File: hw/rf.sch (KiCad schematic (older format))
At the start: 3 parts, among them J8 SMA, U8 HM-TRP-869S

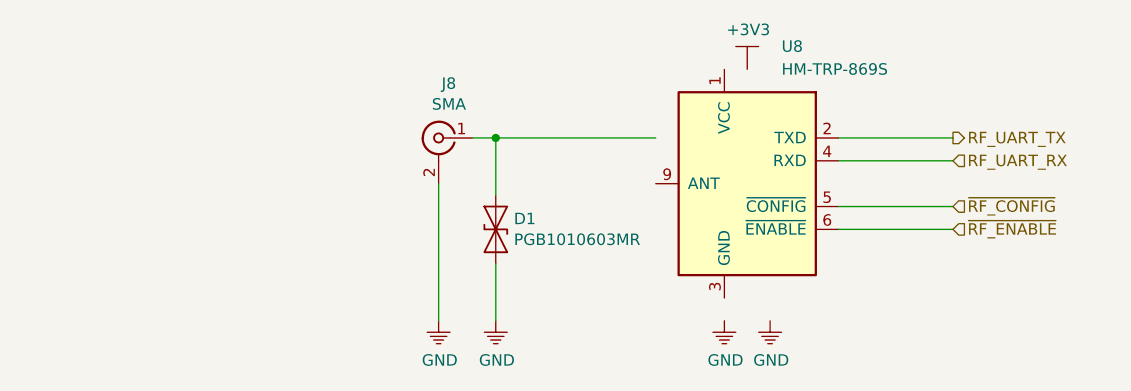
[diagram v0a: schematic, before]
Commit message: updated schematic added footptints
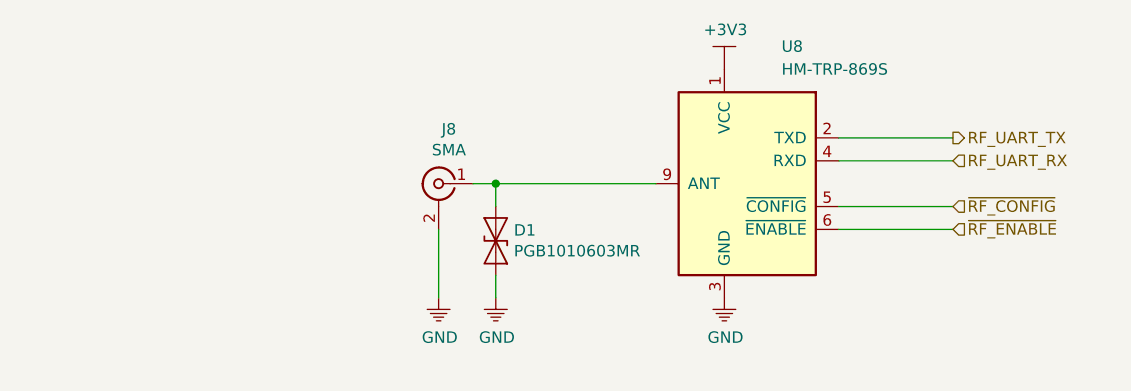
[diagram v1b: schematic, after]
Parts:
- D1: footprint (none) -> Diode_SMD:D_0603_1608Metric
- J8: footprint (none) -> Connector_Coaxial:SMA_Jack_Vertical
- U8: footprint (none) -> KLIB_RF_Module:HM-TRP-SMD
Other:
- moved on the sheet: D1, J8
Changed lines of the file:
@@
 F 0 "U8" H 4100 3200 50  0000 R CNN
 F 1 "HM-TRP-869S" H 4100 3100 50  0000 R CNN
-F 2 "" H 3750 2550 60  0000 C CNN
+F 2 "KLIB_RF_Module:HM-TRP-SMD" H 3750 2550 60  0001 C CNN
 F 3 "https://www.rcscomponents.kiev.ua/datasheets/HM-TRP_433.pdf" V 5050 2650 50  0001 C CNN
 	1    4250 2600
@@
 $EndComp
 $Comp
-L KLIB_Power:GND #PWR056
-U 1 1 5ABFB7B7
-P 4350 3200
-F 0 "#PWR056" H 4350 3000 50  0001 C CNN
-F 1 "GND" H 4355 3027 50  0000 C CNN
-F 2 "" H 4350 3200 50  0001 C CNN
-F 3 "" H 4350 3200 50  0001 C CNN
-	1    4350 3200
-	1    0    0    -1
-$EndComp
-$Comp
 L KLIB_Power:GND #PWR054
 U 1 1 5ABFB811
-P 4150 3200
-F 0 "#PWR054" H 4150 3000 50  0001 C CNN
-F 1 "GND" H 4155 3027 50  0000 C CNN
-F 2 "" H 4150 3200 50  0001 C CNN
-F 3 "" H 4150 3200 50  0001 C CNN
-	1    4150 3200
+P 4150 3100
+F 0 "#PWR054" H 4150 2900 50  0001 C CNN
+F 1 "GND" H 4155 2927 50  0000 C CNN
+F 2 "" H 4150 3100 50  0001 C CNN
+F 3 "" H 4150 3100 50  0001 C CNN
+	1    4150 3100
 	1    0    0    -1
 $EndComp
@@
 L KLIB_Power:+3V3 #PWR055
 U 1 1 5ABFB986
-P 4250 2100
-F 0 "#PWR055" H 4250 1800 50  0001 C CNN
-F 1 "+3V3" H 4255 2273 50  0000 C CNN
-F 2 "" H 4250 2100 50  0001 C CNN
-F 3 "" H 4250 2100 50  0001 C CNN
-	1    4250 2100
+P 4150 2100
+F 0 "#PWR055" H 4150 1800 50  0001 C CNN
+F 1 "+3V3" H 4155 2273 50  0000 C CNN
+F 2 "" H 4150 2100 50  0001 C CNN
+F 3 "" H 4150 2100 50  0001 C CNN
+	1    4150 2100
 	1    0    0    -1
 $EndComp
@@
 L Connector_Specialized:Conn_Coaxial J8
 U 1 1 5ABFBD92
-P 2900 2400
-F 0 "J8" H 2855 2638 50  0000 C CNN
-F 1 "SMA" H 2855 2547 50  0000 C CNN
-F 2 "" H 2900 2400 50  0001 C CNN
-F 3 "" H 2900 2400 50  0001 C CNN
-	1    2900 2400
+P 2900 2600
+F 0 "J8" H 2855 2838 50  0000 C CNN
+F 1 "SMA" H 2855 2747 50  0000 C CNN
+F 2 "Connector_Coaxial:SMA_Jack_Vertical" H 2900 2600 50  0001 C CNN
+F 3 "" H 2900 2600 50  0001 C CNN
+	1    2900 2600
 	-1   0    0    -1
 $EndComp
@@
 L KLIB_Power:GND #PWR052
 U 1 1 5ABFC6C3
-P 2900 3200
-F 0 "#PWR052" H 2900 3000 50  0001 C CNN
-F 1 "GND" H 2905 3027 50  0000 C CNN
-F 2 "" H 2900 3200 50  0001 C CNN
-F 3 "" H 2900 3200 50  0001 C CNN
-	1    2900 3200
+P 2900 3100
+F 0 "#PWR052" H 2900 2900 50  0001 C CNN
+F 1 "GND" H 2905 2927 50  0000 C CNN
+F 2 "" H 2900 3100 50  0001 C CNN
+F 3 "" H 2900 3100 50  0001 C CNN
+	1    2900 3100
 	1    0    0    -1
 $EndComp
 Wire Wire Line
-	2900 3200 2900 2600
+	2900 3100 2900 2800
 Wire Wire Line
-	3050 2400 3150 2400
+	3050 2600 3150 2600
 $Comp
 L Device:D_TVS D1
 U 1 1 5ABFDC8A
-P 3150 2800
-F 0 "D1" V 3104 2879 50  0000 L CNN
-F 1 "PGB1010603MR" V 3195 2879 50  0000 L CNN
-F 2 "" H 3150 2800 50  0001 C CNN
-F 3 "~" H 3150 2800 50  0001 C CNN
-	1    3150 2800
+P 3150 2850
+F 0 "D1" V 3104 2929 50  0000 L CNN
+F 1 "PGB1010603MR" V 3195 2929 50  0000 L CNN
+F 2 "Diode_SMD:D_0603_1608Metric" H 3150 2850 50  0001 C CNN
+F 3 "~" H 3150 2850 50  0001 C CNN
+	1    3150 2850
 	0    1    1    0
 $EndComp
@@
 L KLIB_Power:GND #PWR053
 U 1 1 5ABFEF85
-P 3150 3200
-F 0 "#PWR053" H 3150 3000 50  0001 C CNN
-F 1 "GND" H 3155 3027 50  0000 C CNN
-F 2 "" H 3150 3200 50  0001 C CNN
-F 3 "" H 3150 3200 50  0001 C CNN
-	1    3150 3200
+P 3150 3100
+F 0 "#PWR053" H 3150 2900 50  0001 C CNN
+F 1 "GND" H 3155 2927 50  0000 C CNN
+F 2 "" H 3150 3100 50  0001 C CNN
+F 3 "" H 3150 3100 50  0001 C CNN
+	1    3150 3100
 	1    0    0    -1
 $EndComp
 Wire Wire Line
-	3150 3200 3150 2950
+	3150 3100 3150 3000
 Wire Wire Line
-	3150 2650 3150 2400
-Connection ~ 3150 2400
+	3150 2700 3150 2600
+Connection ~ 3150 2600
 Wire Wire Line
-	3150 2400 3850 2400
+	3150 2600 3850 2600
 Text HLabel 5150 2500 2    50   Input ~ 0
 RF_UART_RX

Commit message: updated schematic
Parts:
- renumbered U8 to U7
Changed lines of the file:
@@
 $EndDescr
 $Comp
-L KLIB_RF_Module:HM-TRP-869S U8
+L KLIB_RF_Module:HM-TRP-869S U7
 U 1 1 5ABE9594
 P 4250 2600
-F 0 "U8" H 4100 3200 50  0000 R CNN
+F 0 "U7" H 4100 3200 50  0000 R CNN
 F 1 "HM-TRP-869S" H 4100 3100 50  0000 R CNN
 F 2 "KLIB_RF_Module:HM-TRP-SMD" H 3750 2550 60  0001 C CNN
@@
 $EndComp
 $Comp
-L KLIB_Power:GND #PWR054
+L KLIB_Power:GND #PWR055
 U 1 1 5ABFB811
 P 4150 3100
-F 0 "#PWR054" H 4150 2900 50  0001 C CNN
+F 0 "#PWR055" H 4150 2900 50  0001 C CNN
 F 1 "GND" H 4155 2927 50  0000 C CNN
 F 2 "" H 4150 3100 50  0001 C CNN
@@
 $EndComp
 $Comp
-L KLIB_Power:+3V3 #PWR055
+L KLIB_Power:+3V3 #PWR054
 U 1 1 5ABFB986
 P 4150 2100
-F 0 "#PWR055" H 4150 1800 50  0001 C CNN
+F 0 "#PWR054" H 4150 1800 50  0001 C CNN
 F 1 "+3V3" H 4155 2273 50  0000 C CNN
 F 2 "" H 4150 2100 50  0001 C CNN

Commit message: placement component to pcb
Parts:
- added C36: 100n, Capacitor_SMD:C_0805_2012Metric, symbol Device:C
- added C37: 1u/50V, Capacitor_SMD:C_0805_2012Metric, symbol Device:C
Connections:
- net +3V3: now also C36.1, C37.1
- net GND: now also C36.2, C37.2
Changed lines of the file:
@@
 Wire Wire Line
 	4650 2800 5150 2800
+$Comp
+L Device:C C37
+U 1 1 5AD84185
+P 1600 2950
+F 0 "C37" H 1715 2996 50  0000 L CNN
+F 1 "1u/50V" H 1715 2905 50  0000 L CNN
+F 2 "Capacitor_SMD:C_0805_2012Metric" H 1638 2800 50  0001 C CNN
+F 3 "~" H 1600 2950 50  0001 C CNN
+	1    1600 2950
+	1    0    0    -1
+$EndComp
+$Comp
+L Device:C C36
+U 1 1 5AD842A5
+P 1150 2950
+F 0 "C36" H 1265 2996 50  0000 L CNN
+F 1 "100n" H 1265 2905 50  0000 L CNN
+F 2 "Capacitor_SMD:C_0805_2012Metric" H 1188 2800 50  0001 C CNN
+F 3 "~" H 1150 2950 50  0001 C CNN
+	1    1150 2950
+	1    0    0    -1
+$EndComp
+$Comp
+L KLIB_Power:GND #PWR091
+U 1 1 5AD8434E
+P 1150 3100
+F 0 "#PWR091" H 1150 2900 50  0001 C CNN
+F 1 "GND" H 1155 2927 50  0000 C CNN
+F 2 "" H 1150 3100 50  0001 C CNN
+F 3 "" H 1150 3100 50  0001 C CNN
+	1    1150 3100
+	1    0    0    -1
+$EndComp
+$Comp
+L KLIB_Power:GND #PWR093
+U 1 1 5AD84379
+P 1600 3100
+F 0 "#PWR093" H 1600 2900 50  0001 C CNN
+F 1 "GND" H 1605 2927 50  0000 C CNN
+F 2 "" H 1600 3100 50  0001 C CNN
+F 3 "" H 1600 3100 50  0001 C CNN
+	1    1600 3100
+	1    0    0    -1
+$EndComp
+Wire Wire Line
+	1600 2800 1600 2750
+Wire Wire Line
+	1600 2750 1400 2750
+Wire Wire Line
+	1150 2750 1150 2800
+$Comp
+L KLIB_Power:+3V3 #PWR092
+U 1 1 5AD8448D
+P 1400 2700
+F 0 "#PWR092" H 1400 2400 50  0001 C CNN
+F 1 "+3V3" H 1405 2873 50  0000 C CNN
+F 2 "" H 1400 2700 50  0001 C CNN
+F 3 "" H 1400 2700 50  0001 C CNN
+	1    1400 2700
+	1    0    0    -1
+$EndComp
+Wire Wire Line
+	1400 2700 1400 2750
+Connection ~ 1400 2750
+Wire Wire Line
+	1400 2750 1150 2750
 $EndSCHEMATC
